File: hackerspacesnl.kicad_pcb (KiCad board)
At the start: 2 copper layers, 79.5 x 95.2 mm, 53 parts, among them J1 Screw_Terminal_01x02, J2 Conn_01x04_Male, Q1 Q_NMOS_GSD, Q2 Q_NMOS_GSD, Q3 Q_NMOS_GSD, Q4 Q_NMOS_GSD, Q5 Q_NMOS_GSD, Q6 Q_NMOS_GSD, SW1 SW_Push, SW2 SW_Push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

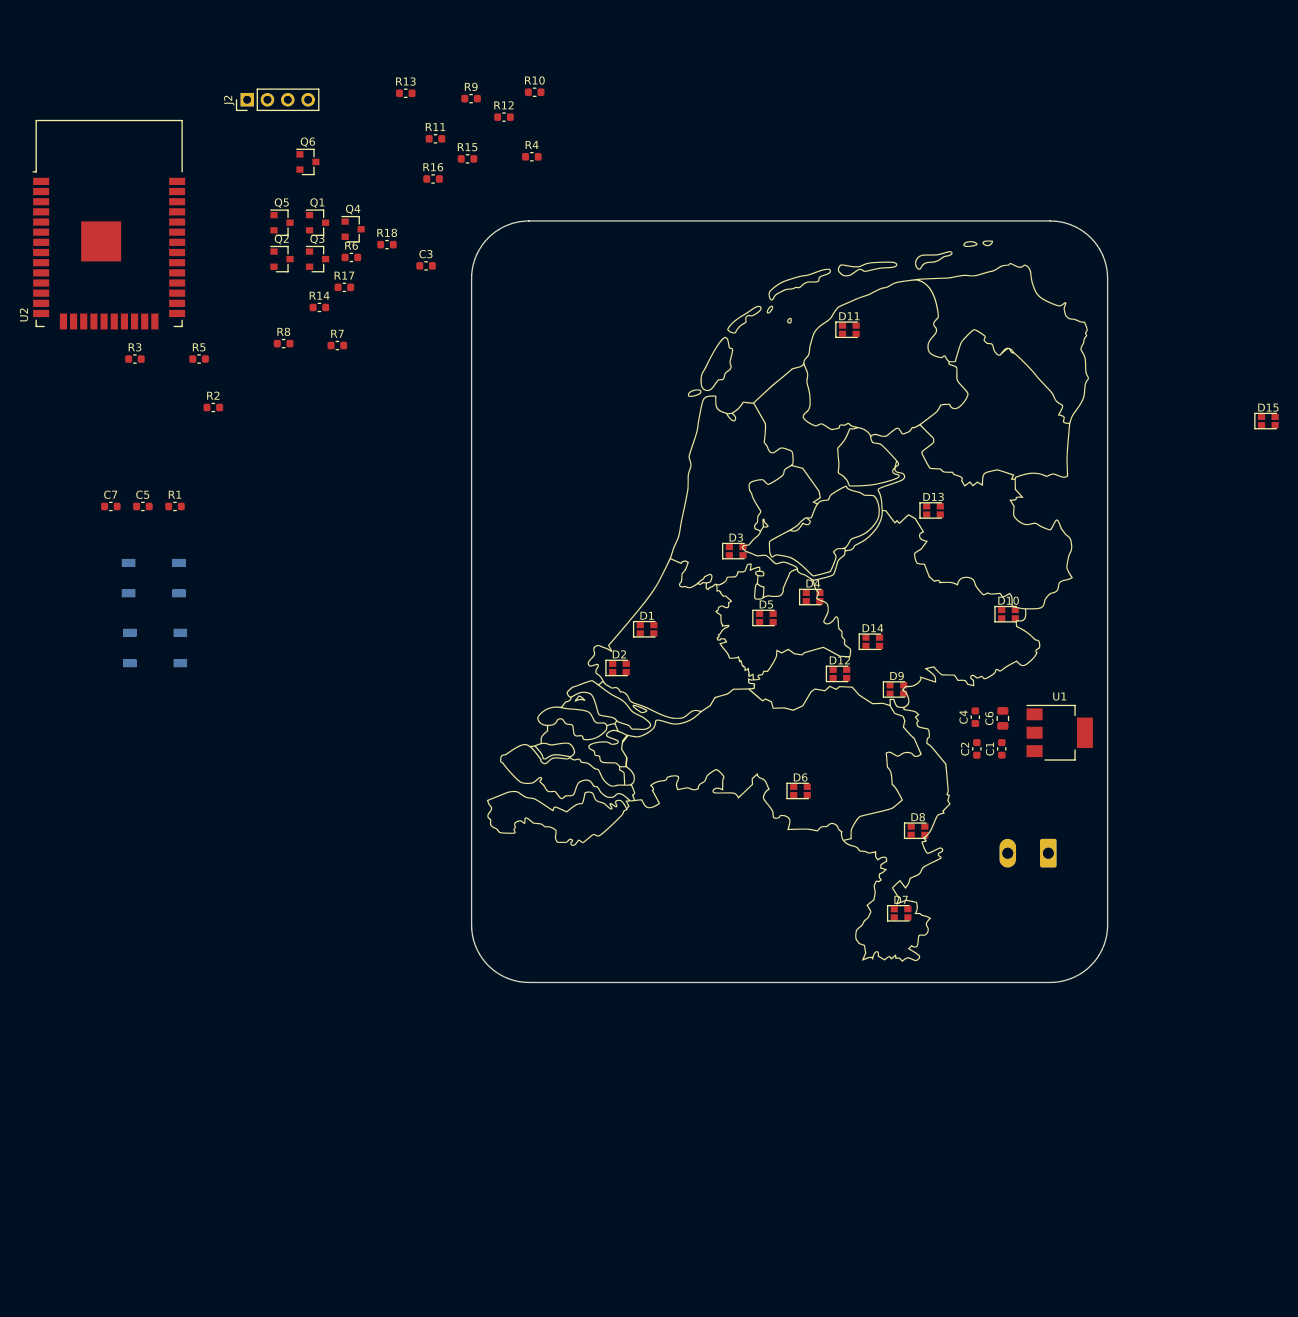
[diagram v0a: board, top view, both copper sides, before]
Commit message: sorted ratsnest, removed map as we will go bigger
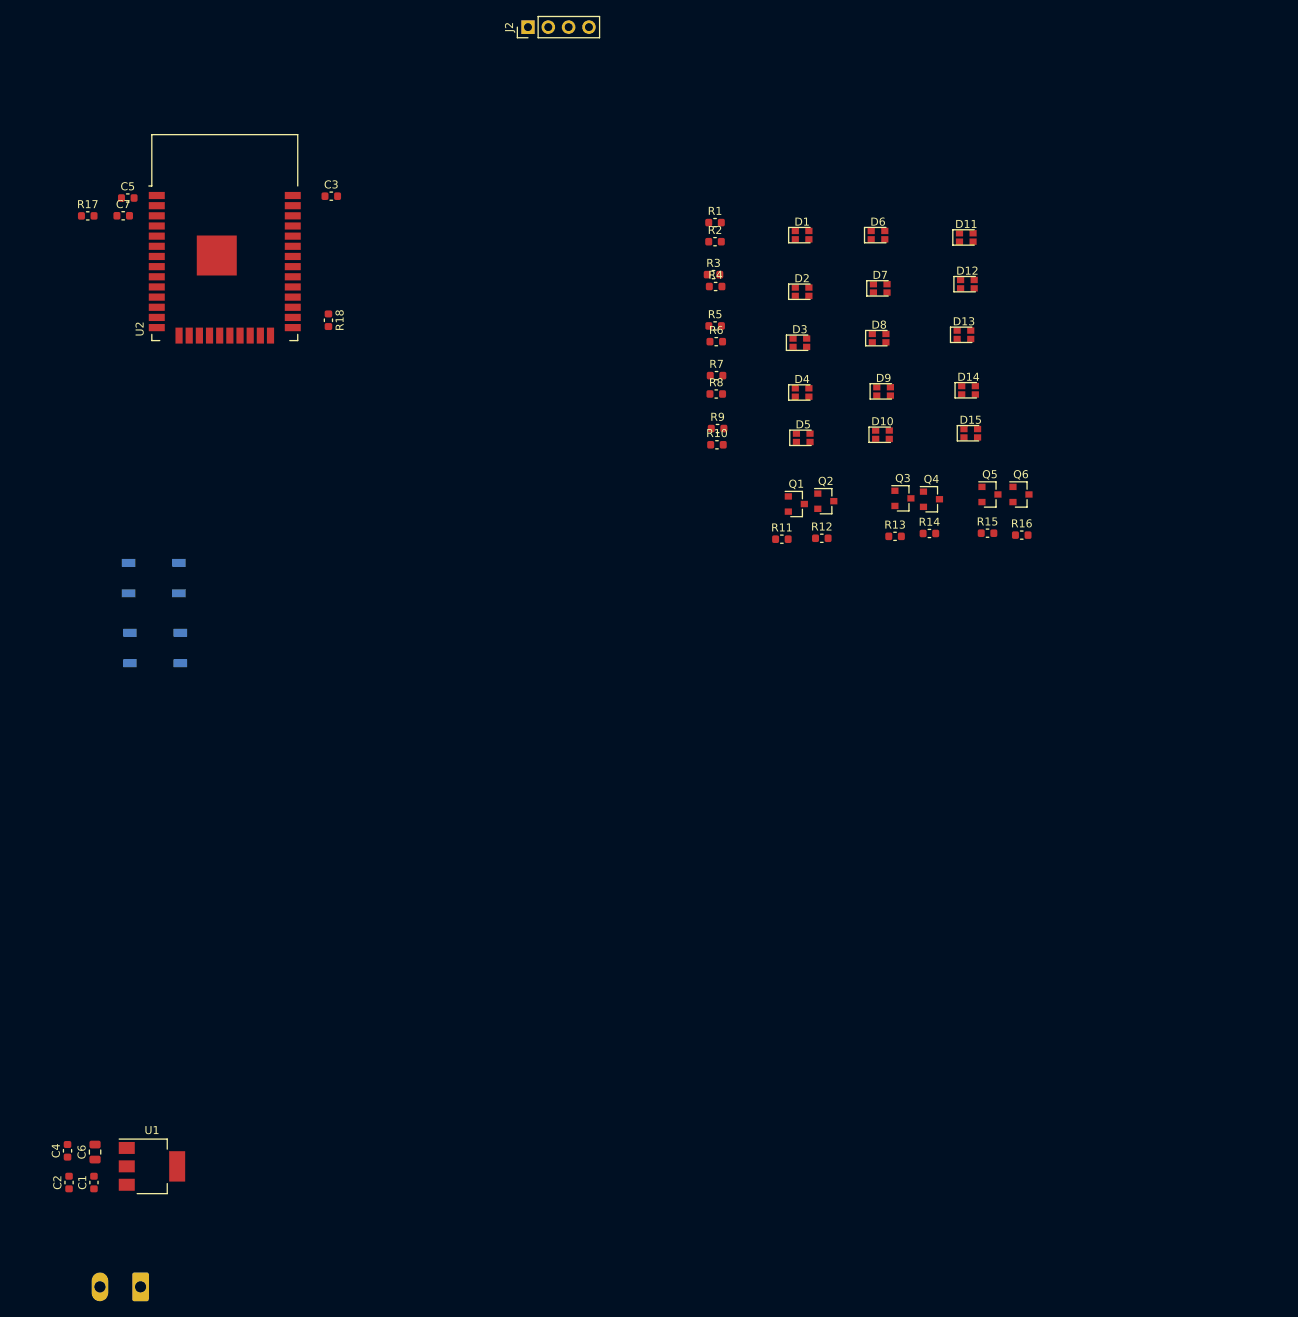
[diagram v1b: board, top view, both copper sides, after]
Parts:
- removed G***: LOGO, hsnl:art
- moved C2 125.8 mm to (26.0, 164.7)
- moved C4 125.8 mm to (25.8, 160.7)
- moved J1 125.8 mm to (35.0, 177.7)
- moved C1 125.8 mm to (29.1, 164.7)
- moved C6 125.8 mm to (29.3, 160.9)
- moved U1 125.8 mm to (36.4, 162.7)
- moved Q6 98.3 mm to (145.0, 78.7)
- moved Q5 94.8 mm to (141.1, 78.7)
- moved R16 86.0 mm to (145.1, 83.8)
- moved R13 82.5 mm to (129.3, 83.9)
- moved R14 81.3 mm to (133.6, 83.6)
- moved R15 80.1 mm to (140.8, 83.5)
- moved Q4 79.8 mm to (133.8, 79.3)
- moved Q3 79.0 mm to (130.2, 79.2)
- moved D7 78.2 mm to (127.4, 52.9)
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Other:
- board outline removed

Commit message: nieuwe svg voor hsnl
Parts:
- SW1, SW2: moved to F.Cu
- moved U2 34.7 mm to (80.1, 51.0)
- moved R18 7.31 mm to (59.7, 64.1)

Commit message: bezig met nieuwe kaart, leds geplaatst en test van traces
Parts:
- added R19: 10K, Resistor_SMD:R_0603_1608Metric, F.Cu at (-39.2, 63.0)
- added R20: 10K, Resistor_SMD:R_0603_1608Metric, F.Cu at (-39.2, 65.5)
- added R21: 10K, Resistor_SMD:R_0603_1608Metric, F.Cu at (-35.2, 63.0)
- added Ref**: Val**, hsnl:hsnl, F.Cu at (97.0, 108.6)
- moved C3 123.8 mm to (-64.5, 30.4)
- moved C5 123.8 mm to (-90.0, 30.6)
- moved C7 123.8 mm to (-90.6, 32.8)
- moved R17 123.8 mm to (-95.0, 32.8)
- moved R18 123.8 mm to (-63.6, 53.1)
- moved SW1 123.8 mm to (-86.7, 78.1)
- moved SW2 123.8 mm to (-86.6, 86.8)
- moved D15 103.8 mm to (120.6, 173.2)
- moved R16 91.0 mm to (103.8, 164.8)
- moved Q6 91.0 mm to (103.7, 159.7)
- moved D14 84.5 mm to (127.1, 149.5)
- moved Q3 79.6 mm to (51.9, 93.4)
- moved Q1 79.6 mm to (38.6, 94.1)
- moved Q2 79.6 mm to (42.3, 93.8)
- moved Q4 79.6 mm to (55.5, 93.5)
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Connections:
- D11 pad 3: Net-(D1-Pad3) -> Net-(D11-Pad3)
- D11 pad 4: Net-(D1-Pad4) -> Net-(D11-Pad4)
- D12 pad 1: Net-(D11-Pad1) -> Net-(D12-Pad1)
- D12 pad 2: Net-(D11-Pad2) -> Net-(D12-Pad2)
- D13 pad 1: Net-(D11-Pad1) -> Net-(D12-Pad1)
- D13 pad 2: Net-(D11-Pad2) -> Net-(D12-Pad2)
- D14 pad 1: Net-(D11-Pad1) -> Net-(D12-Pad1)
- D14 pad 2: Net-(D11-Pad2) -> Net-(D12-Pad2)
- D15 pad 1: Net-(D11-Pad1) -> Net-(D12-Pad1)
- D15 pad 2: Net-(D11-Pad2) -> Net-(D12-Pad2)
- Q5 pad 3: Net-(D11-Pad1) -> Net-(D12-Pad1)
- Q6 pad 3: Net-(D11-Pad2) -> Net-(D12-Pad2)
- U2 pad 14: led_r0 -> Net-(R19-Pad1)
- U2 pad 23: led_r2 -> Net-(R20-Pad1)
- U2 pad 24: led_r3 -> Net-(R21-Pad1)
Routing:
- net Net-(D12-Pad1): track 0.00 -> 95.1 mm
- net Net-(D12-Pad2): track 0.00 -> 90.8 mm
- net Net-(D12-Pad3): track 0.00 -> 56.0 mm, vias 0 -> 2
- net Net-(D12-Pad4): track 0.00 -> 52.0 mm, vias 0 -> 2
- net Net-(D1-Pad3): track 0.00 -> 39.1 mm
- net Net-(D1-Pad4): track 0.00 -> 39.0 mm
- net Net-(D10-Pad2): track 0.00 -> 38.8 mm
- net Net-(D10-Pad1): track 0.00 -> 38.1 mm
- net Net-(D13-Pad3): track 0.00 -> 10.4 mm
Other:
- board outline added: 129.5 x 159.5 mm

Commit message: halverwege component plaatsing
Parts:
- U2: moved to B.Cu
- moved R17 148.2 mm to (42.3, 88.7)
- moved C5 147.1 mm to (38.2, 102.9)
- moved C7 147.1 mm to (37.6, 105.1)
- moved SW1 139.5 mm to (48.9, 110.8)
- moved SW2 139.5 mm to (49.1, 119.5)
- moved C3 121.2 mm to (40.6, 90.7)
- moved R18 120.9 mm to (56.9, 62.6)
- moved R19 106.4 mm to (64.1, 88.0)
- moved R20 103.4 mm to (64.0, 72.4)
- moved R21 99.5 mm to (64.0, 70.9)
- moved R16 76.5 mm to (67.2, 97.6)
- moved Q6 76.5 mm to (67.1, 92.5)
- moved Q2 2.78 mm to (45.0, 94.2)
- moved Q1 2.33 mm to (40.9, 94.3)
- moved Q3 1.05 mm to (51.2, 94.2)
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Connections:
- U2 pad 16: led_r1 -> Net-(U2-Pad16)
- U2 pad 26: led_r4 -> Net-(U2-Pad26)
- U2 pad 28: led_c5 -> Net-(U2-Pad28)
- U2 pad 29: led_c4 -> Net-(U2-Pad29)
- U2 pad 30: led_c3 -> Net-(U2-Pad30)
- U2 pad 31: led_c2 -> Net-(U2-Pad31)
- U2 pad 33: led_c1 -> Net-(U2-Pad33)
- U2 pad 36: led_c0 -> Net-(U2-Pad36)
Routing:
- net Net-(D12-Pad1): track 95.1 -> 0.00 mm
- net Net-(D12-Pad2): track 90.8 -> 0.00 mm
- net Net-(D12-Pad3): track 56.0 -> 0.00 mm, vias 2 -> 0
- net Net-(D12-Pad4): track 52.0 -> 0.00 mm, vias 2 -> 0
- net Net-(D1-Pad3): track 39.1 -> 0.00 mm
- net Net-(D1-Pad4): track 39.0 -> 0.00 mm
- net Net-(D10-Pad2): track 38.8 -> 0.00 mm
- net Net-(D10-Pad1): track 38.1 -> 0.00 mm
- net Net-(D13-Pad3): track 10.4 -> 0.08 mm

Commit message: update
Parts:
- removed C7: 100nF, Capacitor_SMD:C_0603_1608Metric
- SW1, SW2: moved to B.Cu
- moved Q6 83.2 mm to (111.1, 163.2)
- moved Q5 81.7 mm to (104.6, 163.1)
- moved R16 76.2 mm to (107.9, 162.1), turned to 180 degrees
- moved R15 75.2 mm to (101.5, 162.1), turned to 180 degrees
- moved C2 75.2 mm to (146.2, 141.8), turned to 180 degrees
- moved C1 73.0 mm to (146.2, 138.7), turned to 180 degrees
- moved Q3 72.7 mm to (82.9, 159.6)
- moved Q4 72.7 mm to (87.1, 159.6)
- moved R13 72.6 mm to (82.7, 163.5)
- moved R14 72.5 mm to (86.9, 163.6)
- moved C4 70.6 mm to (142.3, 142.0), turned to 180 degrees
- moved R11 68.3 mm to (67.9, 159.3)
- moved C6 68.2 mm to (142.4, 138.6), turned to 180 degrees
- moved R12 68.0 mm to (72.0, 159.3)
- moved J1 67.9 mm to (146.8, 151.9)
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
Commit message: layout almost done
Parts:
- removed R19, R20, R21: 10K, Resistor_SMD:R_0603_1608Metric
- D4: value Red-GreenLED-parts -> Red-GreenLED
- J2: footprint Connector_PinHeader_2.54mm:PinHeader_1x04_P2.54mm_Vertical -> Connector_PinHeader_2.54mm:PinHeader_1x04_P2.54mm_Vertical_SMD_Pin1Left; moved to B.Cu
- moved R18 22.8 mm to (44.0, 72.7), turned to 0 degrees
- moved R17 21.1 mm to (44.0, 71.2)
- moved C5 17.3 mm to (40.7, 72.7)
- moved C3 17.3 mm to (40.7, 71.2)
- moved Q4 7.13 mm to (92.3, 154.8)
- moved R13 7.13 mm to (87.9, 158.7)
- moved R14 7.13 mm to (92.1, 158.7)
- moved Q3 7.13 mm to (88.1, 154.8)
- moved R15 6.71 mm to (107.2, 165.6), turned to 0 degrees
- moved R16 4.80 mm to (111.1, 165.7), turned to 0 degrees
- moved J2 4.43 mm to (39.9, 57.2), turned to 270 degrees
- moved Q5 2.48 mm to (107.1, 163.1)
- moved Q1 2.32 mm to (67.7, 153.3)
- moved Q2 2.32 mm to (71.8, 153.3)
- moved R11 2.32 mm to (67.7, 157.0)
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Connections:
- J2 pad 1: +5V -> +3V3
- U2 pad 10: Net-(U2-Pad10) -> led_r4
- U2 pad 26: Net-(U2-Pad26) -> led_c0
- U2 pad 27: Net-(U2-Pad27) -> led_c1
- U2 pad 28: Net-(U2-Pad28) -> led_c2
- U2 pad 29: Net-(U2-Pad29) -> led_c3
- U2 pad 30: Net-(U2-Pad30) -> led_c4
- U2 pad 31: Net-(U2-Pad31) -> led_c5
- U2 pad 6: Net-(U2-Pad6) -> led_r0
- U2 pad 7: Net-(U2-Pad7) -> led_r1
- U2 pad 8: Net-(U2-Pad8) -> led_r2
- U2 pad 9: Net-(U2-Pad9) -> led_r3
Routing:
- net +3V3: track 0.00 -> 285.5 mm, vias 0 -> 3
- net Net-(D1-Pad1): track 0.00 -> 145.4 mm, vias 0 -> 7
- net Net-(D1-Pad2): track 0.00 -> 143.2 mm, vias 0 -> 6
- net led_c5: track 0.00 -> 138.4 mm, vias 0 -> 1
- net led_c4: track 0.00 -> 132.0 mm, vias 0 -> 1
- net Net-(D12-Pad1): track 0.00 -> 115.2 mm, vias 0 -> 7
- net led_c3: track 0.00 -> 114.7 mm, vias 0 -> 1
- net Net-(D12-Pad2): track 0.03 -> 114.7 mm, vias 0 -> 6
- net Net-(D10-Pad1): track 0.00 -> 109.3 mm, vias 0 -> 8
- net led_c2: track 0.00 -> 108.1 mm, vias 0 -> 1
- net Net-(D10-Pad2): track 0.05 -> 104.4 mm, vias 0 -> 8
- net Net-(D12-Pad3): track 0.00 -> 102.9 mm, vias 0 -> 7
- net Net-(D14-Pad3): track 0.00 -> 98.1 mm, vias 0 -> 10
- net Net-(D14-Pad4): track 0.00 -> 97.1 mm, vias 0 -> 7
- net Net-(D12-Pad4): track 0.00 -> 96.3 mm, vias 0 -> 8
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- added copper zone on B.Cu, net GND
- added copper zone on F.Cu, net GND

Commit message: back silk text and holes added
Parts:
- added REF**: MountingHole_3.2mm_M3, MountingHole:MountingHole_3.2mm_M3, F.Cu at (39.2, 181.2)
- added REF**: MountingHole_3.2mm_M3, MountingHole:MountingHole_3.2mm_M3, F.Cu at (154.7, 181.4)
- added REF**: MountingHole_3.2mm_M3, MountingHole:MountingHole_3.2mm_M3, F.Cu at (154.7, 36.0)
- added REF**: MountingHole_3.2mm_M3, MountingHole:MountingHole_3.2mm_M3, F.Cu at (40.1, 36.5)
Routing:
- net Net-(D10-Pad1): track 109.3 -> 107.6 mm
- net Net-(D14-Pad3): track 98.1 -> 99.1 mm
- net GND: vias 22 -> 36
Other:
- board text added: "2009: RandomData (Utrecht) 2009: RevSpace (Den Haag) 2010: Hack42 (Arnhem) 2010-2017: Sk1llz (Almere) 2010: ACKspace (Heerlen) 2011: TkkrLab (Enschede) 2011: Bitlair (Amersfoort) 2011: Frack (Leeuwarden) 2011: TechInc (Amsterdam) 2012: NURDspace (Wageningen) 2014: TDvenlo (Venlo dus) 2015: Pixelbar (Rotterdam) 2018: Hackerspace Nijmegen (Nijmegen dus) 2018: Hackalot (Eindhoven)"
- board text added: "3.3v GND RX TX"
- board text added: "Flash"
- board text added: "Reset"
- board text added: "hoera10jaar 2020-01-25 CC-BY-NC Stichting Revelation Space Hackerspace Den Haag Makerspace Leidschendam"

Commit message: klaar op refs na
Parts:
- added Ref**: Val**, hsnl:revspace_logo, B.Cu at (138.0, 173.7)
